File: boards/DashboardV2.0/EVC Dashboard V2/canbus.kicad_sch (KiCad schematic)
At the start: 0 parts

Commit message: Dashboard schematic changes
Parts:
- added C3, C4: 0.1uF, symbol Device:C
- added U3: ISO1042BDWVR, DWV0008A, symbol ISO1042BDWVR:ISO1042BDWVR
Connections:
- new net: C4.2, U3.8 (VCC2)
- new net +3.3V: C3.2, U3.1 (VCC1)
- new net CAN_H: U3.7 (CANH)
- new net CAN_L: U3.6 (CANL)
- new net CAN_RX: U3.3 (RXD)
- new net CAN_TX: U3.2 (TXD)
- new net GND: C3.1, C4.1, U3.4 (GND1), U3.5 (GND2)
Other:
- note added: "What voltage does Vcc2 connect to?"

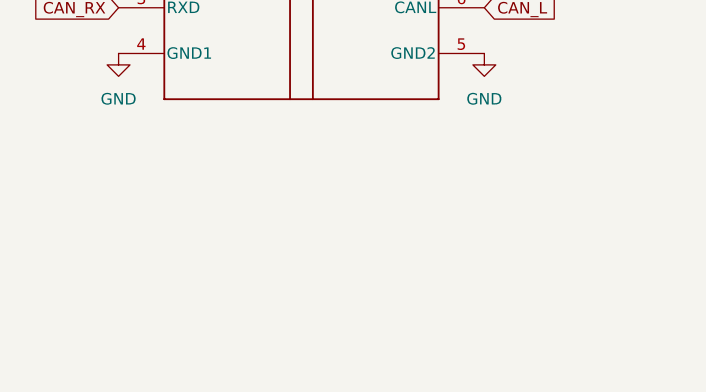
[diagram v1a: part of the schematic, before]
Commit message: Added oscillators and ferrite bead to MCU
Added the remaining MCU parts, will add NC and LED_CAN to finish MCU connections
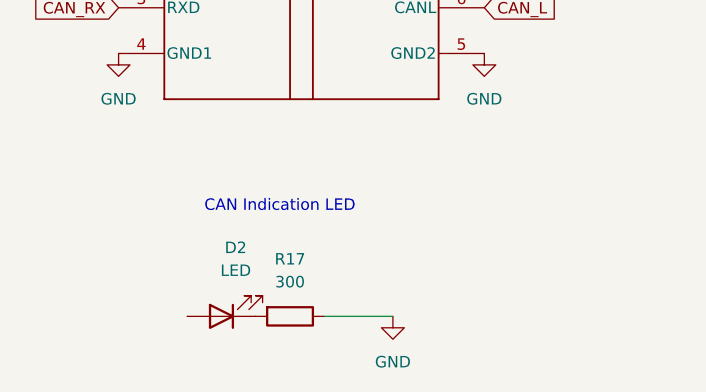
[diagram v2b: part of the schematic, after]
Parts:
- added D2: LED, LED_SMD:LED_0603_1608Metric, symbol Device:LED
- added R17: 300, Resistor_SMD:R_0805_2012Metric, symbol Device:R
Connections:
- net GND: now also R17.1
- new net: D2.1 (K), R17.2
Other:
- note added: "CAN Indication LED"

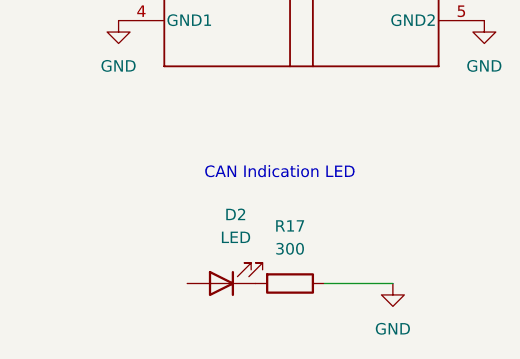
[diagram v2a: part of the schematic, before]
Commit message: Added MCU Labels
Finished adding labels for LEDs and CAN indicator LED
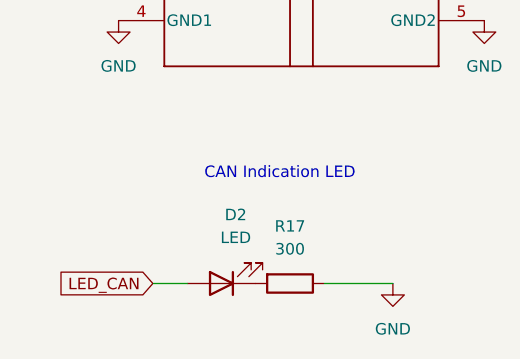
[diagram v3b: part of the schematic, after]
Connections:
- net LED_CAN: now reaches D2.2 (A)
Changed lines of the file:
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@@
+		)
+	)
+	(wire
+		(pts
+			(xy 43.18 80.01) (xy 46.99 80.01)
+		)
+		(stroke
+			(width 0)
+			(type default)
 		)
 	)
@@
 			)
 		)
+	)
+	(global_label "LED_CAN"
+		(shape input)
+		(at 43.18 80.01 180)
+		(fields_autoplaced yes)
+		(effects
+			(font
+				(size 1.27 1.27)
+			)
+			(justify right)
+		)
+		(property "Intersheetrefs" "${INTERSHEET_REFS}"
+			(at 32.091 80.01 0)
+			(hide yes)
+			(show_name no)
+			(do_not_autoplace no)
+			(effects
+				(font
+					(size 1.27 1.27)
+				)
+				(justify right)
+			)
+		)

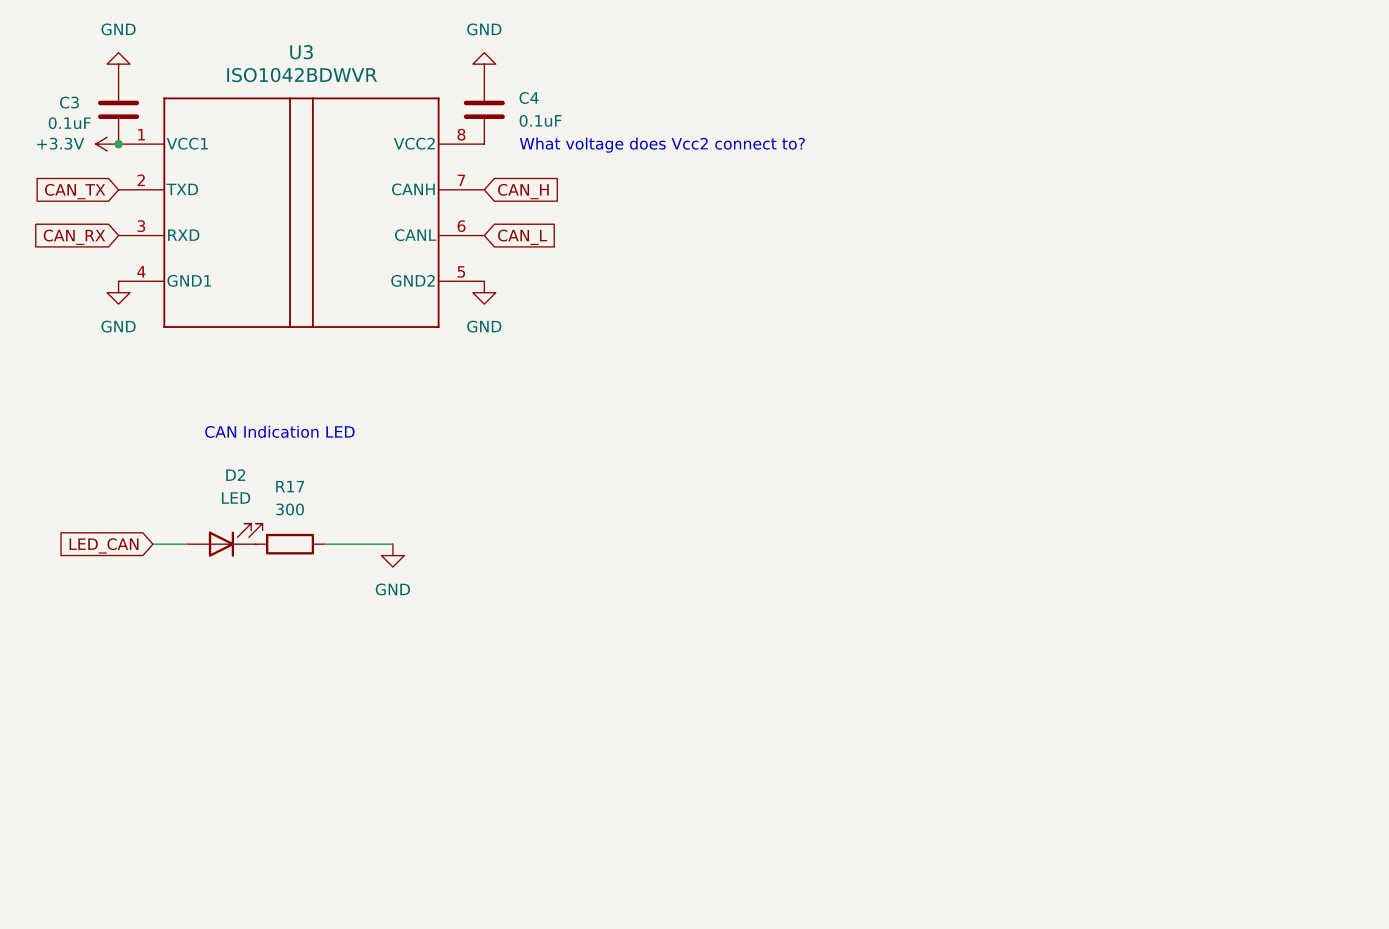
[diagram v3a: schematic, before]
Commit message: Added can connector
Added can connector and connections, fixed transciever connections
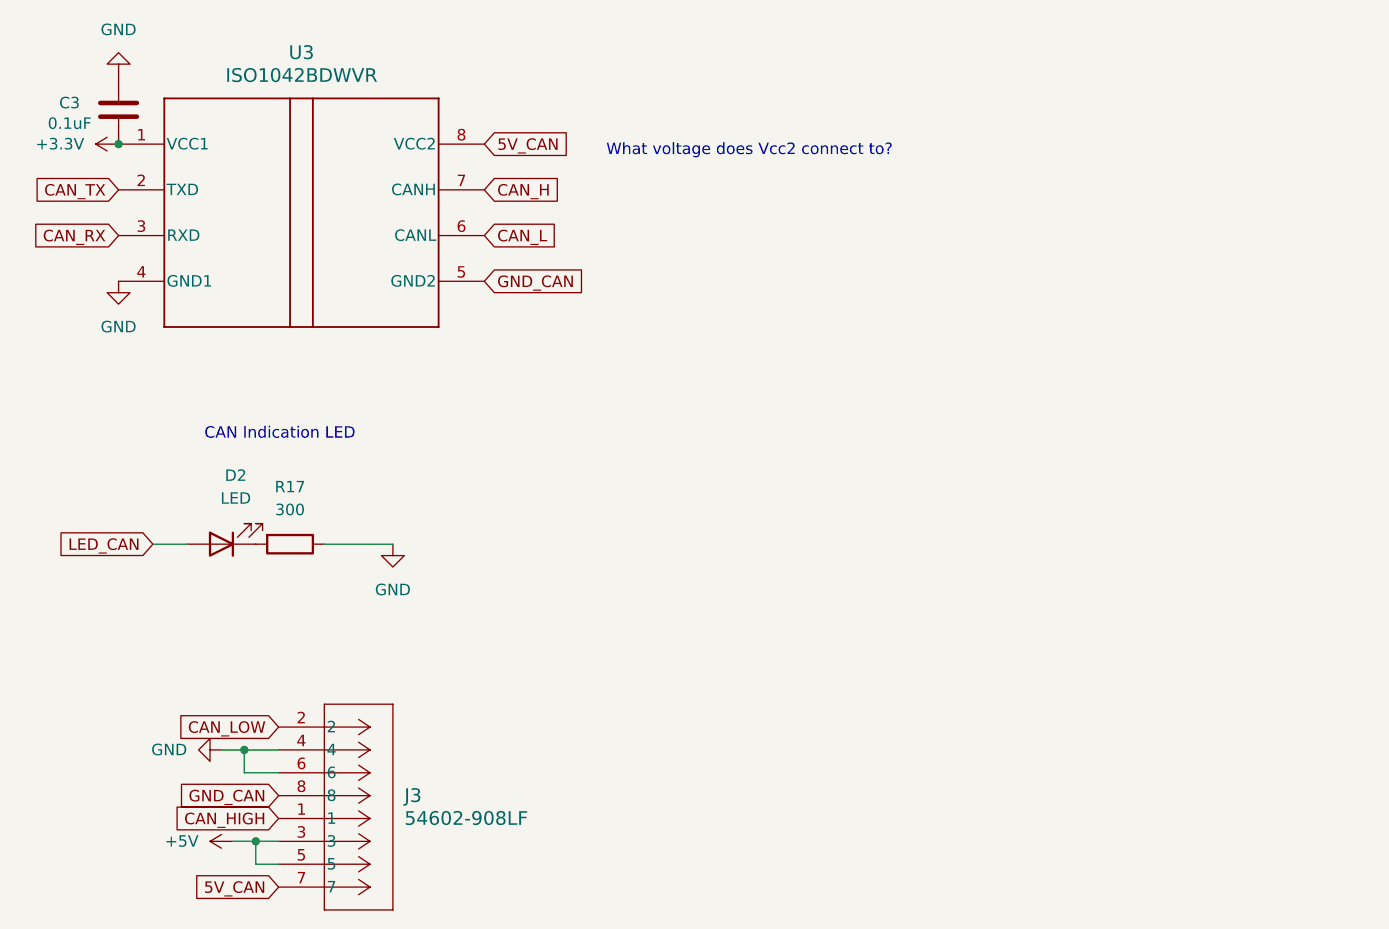
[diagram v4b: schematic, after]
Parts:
- removed C4: 0.1uF, symbol Device:C
- added J3: 54602-908LF, CONN8_2-908LF_AMP, symbol Regulators:54602-908LF
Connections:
- net GND: now also J3.4, J3.6; no longer U3.5 (GND2)
- net 5V_CAN: now reaches U3.8 (VCC2)
- net 5V_CAN: now also J3.7
- new net +5V: J3.3, J3.5
- new net CAN_HIGH: J3.1
- new net CAN_LOW: J3.2
- new net GND_CAN: J3.8, U3.5 (GND2)

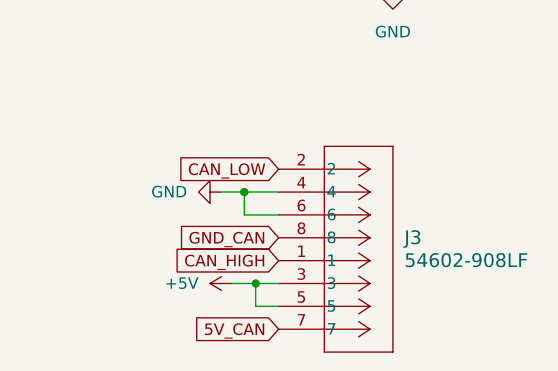
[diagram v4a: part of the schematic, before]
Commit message: minor changes to overvoltage protection + comments
changed overvoltage protection chip wiring to better match application in datasheet, also created 5V unlimit input to separate connected 5V to the 5V running through the board (output from overvoltage circuit). also added comments on overvoltage circuit and stlink regarding confusions
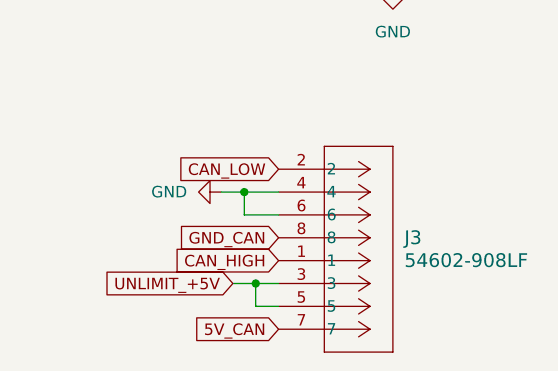
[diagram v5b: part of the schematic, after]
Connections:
- net +5V renamed UNLIMIT_+5V
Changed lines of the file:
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@@
+		)
+	)
+	(global_label "UNLIMIT_+5V"
+		(shape input)
+		(at 52.07 113.03 180)
+		(fields_autoplaced yes)
+		(effects
+			(font
+				(size 1.27 1.27)
+			)
+			(justify right)
+		)
+		(property "Intersheetrefs" "${INTERSHEET_REFS}"
+			(at 36.929 113.03 0)
+			(hide yes)
+			(show_name no)
+			(do_not_autoplace no)
+			(effects
+				(font
+					(size 1.27 1.27)
+				)
+				(justify right)
+			)
 		)
 	)
@@
 					(unit 1)
 				)
-			)
-		)
-	)
-	(symbol
-		(lib_id "power:+5V")
-		(at 52.07 113.03 90)
-		(unit 1)
-		(body_style 1)
-		(exclude_from_sim no)
-		(in_bom yes)
-		(on_board yes)
-		(in_pos_files yes)
-		(dnp no)
-		(fields_autoplaced yes)
-		(property "Reference" "#PWR012"
-			(at 55.88 113.03 0)
-			(hide yes)
-			(show_name no)
-			(do_not_autoplace no)
-			(effects
-				(font
-					(size 1.27 1.27)
-				)
-			)
-		)
-		(property "Value" "+5V"
-			(at 48.26 113.0299 90)
-			(show_name no)
-			(do_not_autoplace no)
-			(effects
-				(font
-					(size 1.27 1.27)
-				)
-				(justify left)
-			)
-		)
-		(property "Footprint" ""
-			(at 52.07 113.03 0)
-			(hide yes)
-			(show_name no)
-			(do_not_autoplace no)
-			(effects
-				(font
-					(size 1.27 1.27)
-				)
-			)
-		)
-		(property "Datasheet" ""
-			(at 52.07 113.03 0)
-			(hide yes)
-			(show_name no)
-			(do_not_autoplace no)
-			(effects
-				(font
-					(size 1.27 1.27)
-				)
-			)
-		)
-		(property "Description" "Power symbol creates a global label with name \"+5V\""
-			(at 52.07 113.03 0)
-			(hide yes)
-			(show_name no)
-			(do_not_autoplace no)
-			(effects
-				(font
-					(size 1.27 1.27)
-				)
-			)
-		)
-		(pin "1"
-		)
-		(instances
-			(project "EVC Dashboard V2"
-				(path "/ede78d5d-1d5c-4e8d-a13e-c039265851a9/72b4ce4a-b1c7-4d06-b603-11de841c74d6"
-					(reference "#PWR012")
-					(unit 1)
-				)

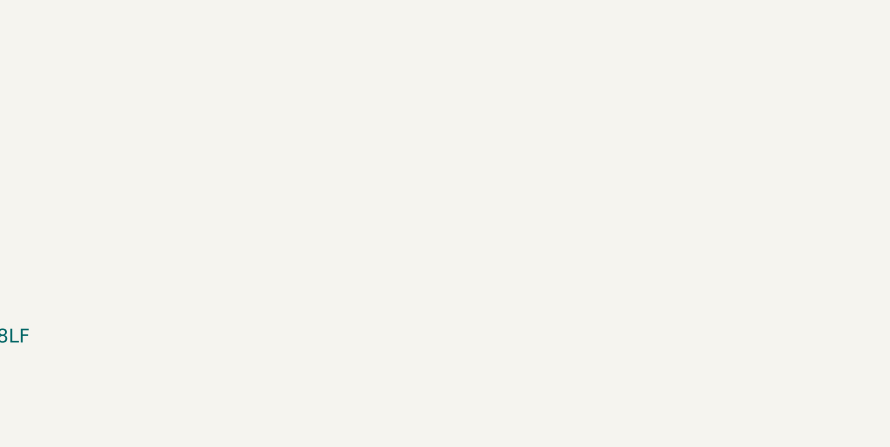
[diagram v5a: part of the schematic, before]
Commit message: Can connector
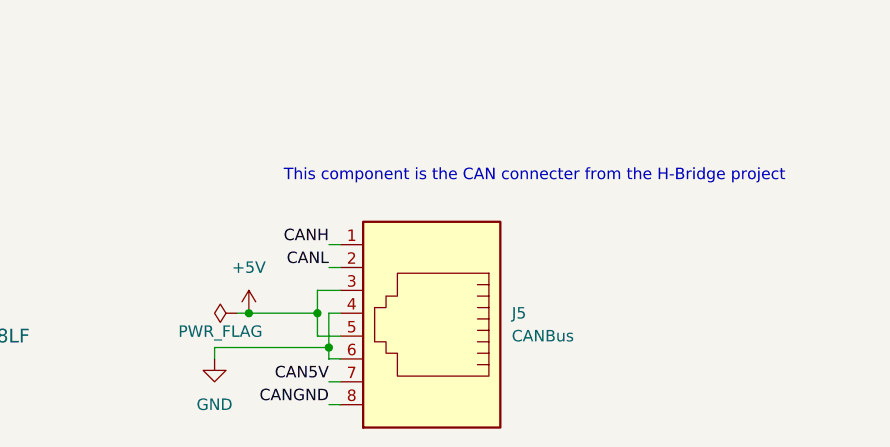
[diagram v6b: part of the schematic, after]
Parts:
- added J5: CANBus, Connector_RJ:RJ45_Amphenol_54602-x08_Horizontal, symbol Connector:RJ45
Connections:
- net GND: now also J5.4, J5.6
- new net +5V: J5.3, J5.5
- new net CAN5V: J5.7
- new net CANGND: J5.8
- new net CANH: J5.1
- new net CANL: J5.2
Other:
- note added: "This component is the CAN connecter from the H-Bridge project"
